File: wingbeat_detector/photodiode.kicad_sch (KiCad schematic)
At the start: 5 parts, among them U4 OPA381

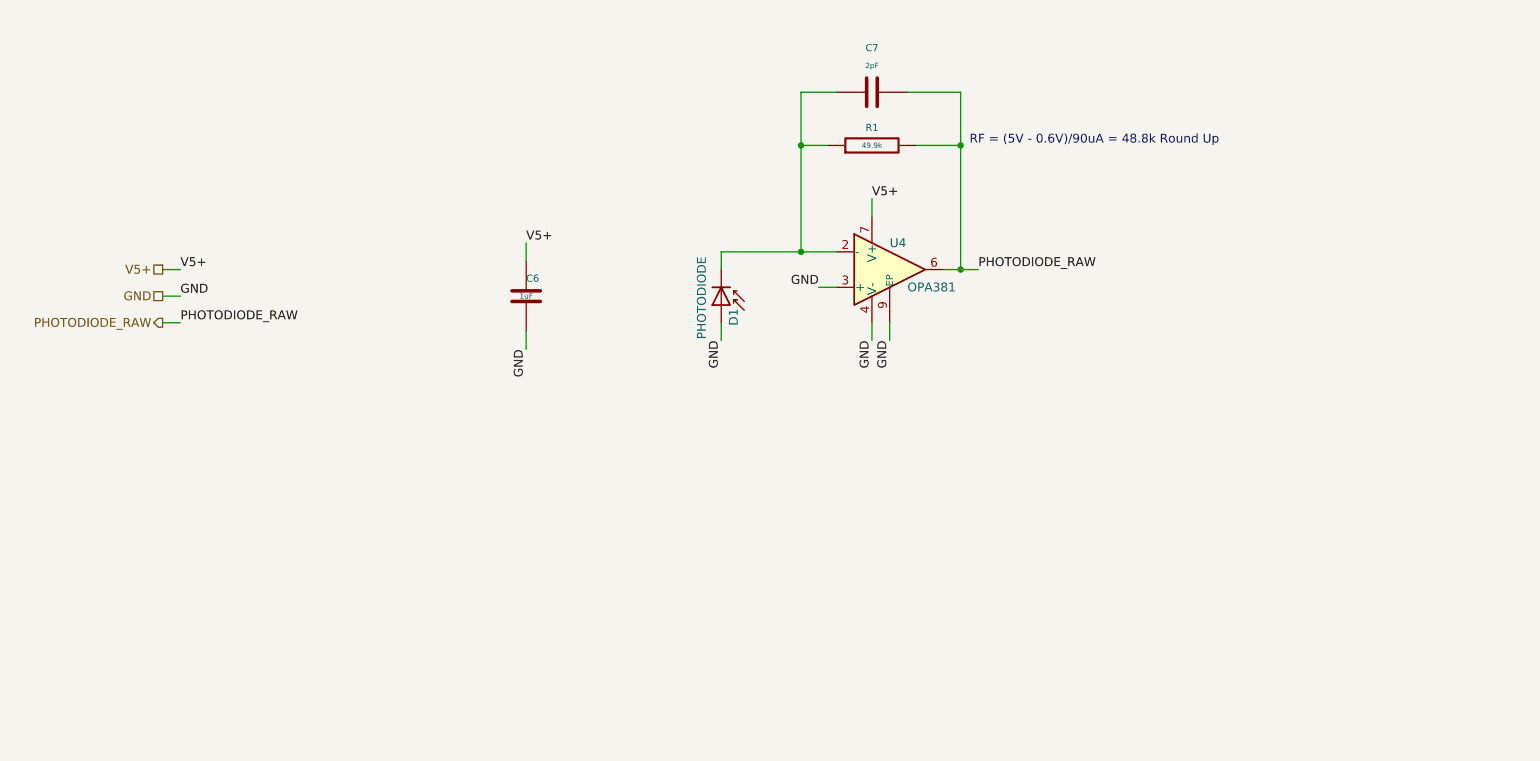
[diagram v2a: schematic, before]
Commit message: Add buffered output
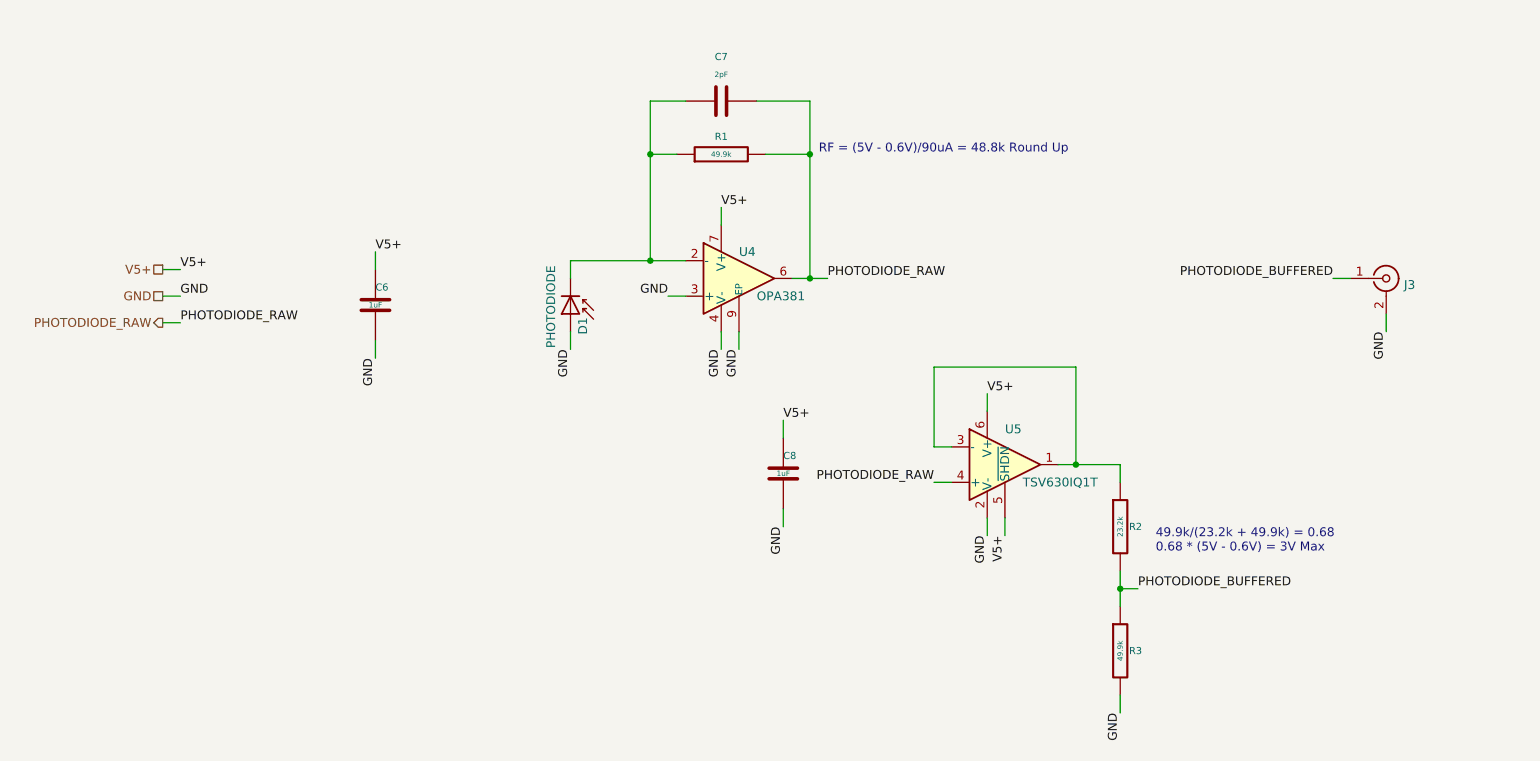
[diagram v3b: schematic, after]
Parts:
- added C8: 1uF, Janelia:C_0402_1005Metric, symbol Janelia:C_1uF_0402
- added J3: CONN_UMC_JACK_SMD, Janelia:UMC_AMPHENOL_A-1JB, symbol Janelia:CONN_UMC_JACK_SMD
- added R2: 23.2k, Janelia:R_0402_1005Metric, symbol Janelia:R_23.2k_0402
- added R3: 49.9k, Janelia:R_0402_1005Metric, symbol Janelia:R_49.9k_0402
- added U5: TSV630IQ1T, Janelia:PSON40P120X130X50-6N, symbol Janelia:TSV630IQ1T
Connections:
- net GND: now also C8.2, J3.2 (Ext), R3.2, U5.2 (V-)
- net PHOTODIODE_RAW: now also U5.4 (+)
- net V5+: now also C8.1, U5.5 (~{SHDN}), U5.6 (V+)
- new net: R2.1, U5.1, U5.3 (-)
- new net PHOTODIODE_BUFFERED: J3.1 (In), R2.2, R3.1
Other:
- note added: "49.9k/(23.2k + 49.9k) = 0.68 0.68 * (5V - 0.6V) = 3V Max"
- company: (none) -> Howard Hughes Medical Institute
- title: (none) -> wingbeat_detector
- moved on the sheet: C6, C7, D1, R1, U4

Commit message: Initial schematic layout
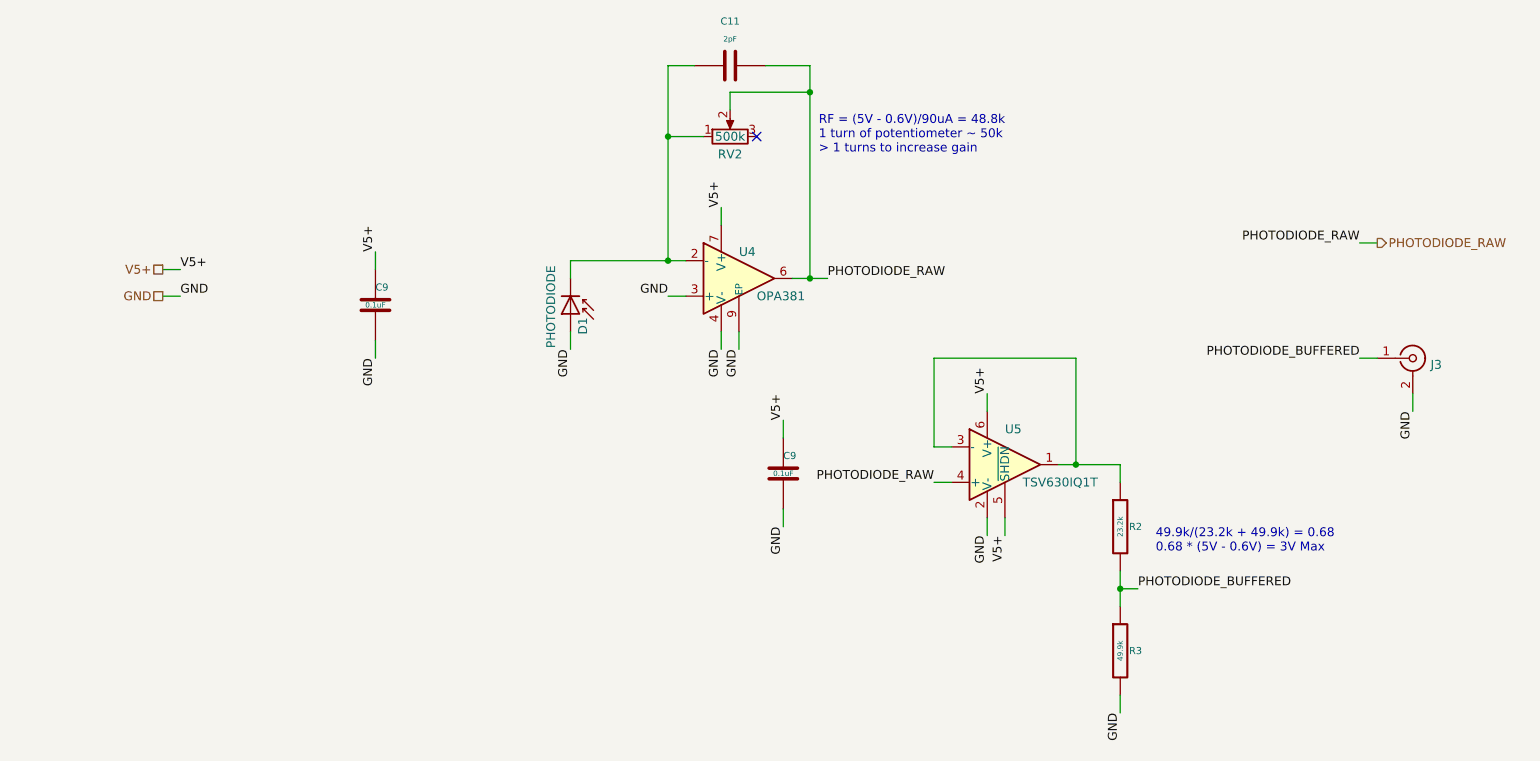
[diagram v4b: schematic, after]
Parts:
- removed C6, C8: 1uF, Janelia:C_0402_1005Metric, symbol Janelia:C_1uF_0402
- removed R1: 49.9k, Janelia:R_0402_1005Metric, symbol Janelia:R_49.9k_0402
- added C9 (x2): 0.1uF, Janelia:C_0402_1005Metric, symbol Janelia:C_0.1uF_0402
- added RV2: 500k, Janelia:Potentiometer_Bourns_3223W_Vertical, symbol Janelia:R_Potentiometer_500k_3.9x3.18mm_11turn_Vertical
- renumbered C7 to C11
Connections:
- net GND: now also C9.2, C9.2
- net PHOTODIODE_RAW: now also RV2.2
- net V5+: now also C9.1, C9.1
- net at C11.1, D1.1 (K), U4.2 (-): now also RV2.1
- no-connect marks 0 -> 1
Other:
- note added: "RF = (5V - 0.6V)/90uA = 48.8k 1 turn of potentiometer ~ 50k > 1 turns to increase gain"
- note removed: "RF = (5V - 0.6V)/90uA = 48.8k Round Up"
- moved on the sheet: C11, J3

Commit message: Double check schematic
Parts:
- added R3 (x3): 49.9k, Janelia:R_0402_1005Metric, symbol Janelia:R_49.9k_0402
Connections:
- net GND: now also R3.1
- net PHOTODIODE_RAW: now also R3.2
- new net: R3.1, R3.1, R3.2
- new net V10-: R3.2
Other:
- note added: "Optional pulldown resistor to ~ -5V to extend output voltage range to include 0V"
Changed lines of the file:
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@@
   (junction (at 186.69 111.76) (diameter 0) (color 0 0 0 0)
+  )
+  (junction (at 86.36 125.73) (diameter 0) (color 0 0 0 0)
   )
   (junction (at 128.27 64.77) (diameter 0) (color 0 0 0 0)
@@
     (stroke (width 0) (type default))
   )
+  (wire (pts (xy 86.36 125.73) (xy 86.36 128.27))
+    (stroke (width 0) (type default))
+  )
   (wire (pts (xy 138.43 92.71) (xy 138.43 95.25))
     (stroke (width 0) (type default))
@@
     (stroke (width 0) (type default))
   )
+  (wire (pts (xy 101.6 125.73) (xy 104.14 125.73))
+    (stroke (width 0) (type default))
+  )
   (wire (pts (xy 132.08 54.61) (xy 128.27 54.61))
     (stroke (width 0) (type default))
@@
     (stroke (width 0) (type default))
   )
+  (wire (pts (xy 55.88 91.44) (xy 58.42 91.44))
+    (stroke (width 0) (type default))
+  )
   (wire (pts (xy 173.99 104.14) (xy 173.99 101.6))
     (stroke (width 0) (type default))
@@
     (stroke (width 0) (type default))
   )
+  (wire (pts (xy 86.36 140.97) (xy 86.36 143.51))
+    (stroke (width 0) (type default))
+  )
   (wire (pts (xy 173.99 119.38) (xy 173.99 121.92))
     (stroke (width 0) (type default))
   )
+  (wire (pts (xy 86.36 123.19) (xy 86.36 125.73))
+    (stroke (width 0) (type default))
+  )
   (wire (pts (xy 186.69 111.76) (xy 193.04 111.76))
     (stroke (width 0) (type default))
@@
   )
   (wire (pts (xy 114.3 82.55) (xy 128.27 82.55))
+    (stroke (width 0) (type default))
+  )
+  (wire (pts (xy 86.36 110.49) (xy 86.36 107.95))
+    (stroke (width 0) (type default))
+  )
+  (wire (pts (xy 86.36 125.73) (xy 88.9 125.73))
     (stroke (width 0) (type default))
   )
@@
     (effects (font (size 1.27 1.27)) (justify left bottom))
   )
+  (text "Optional pulldown resistor to ~ -5V\nto extend output voltage range to \ninclude 0V"
+    (at 92.71 135.89 0)
+    (effects (font (size 1.27 1.27)) (justify left bottom))
+  )
   (label "V5+" (at 135.89 74.93 90) (fields_autoplaced)
     (effects (font (size 1.27 1.27)) (justify left bottom))
@@
     (effects (font (size 1.27 1.27)) (justify right bottom))
   )
+  (label "PHOTODIODE_RAW" (at 104.14 125.73 0) (fields_autoplaced)
+    (effects (font (size 1.27 1.27)) (justify left bottom))
+  )
   (label "V5+" (at 86.36 81.28 90) (fields_autoplaced)
     (effects (font (size 1.27 1.27)) (justify left bottom))
@@
     (effects (font (size 1.27 1.27)) (justify right bottom))
   )
+  (label "V10-" (at 86.36 143.51 270) (fields_autoplaced)
+    (effects (font (size 1.27 1.27)) (justify right bottom))
+  )
   (label "GND" (at 86.36 96.52 270) (fields_autoplaced)
     (effects (font (size 1.27 1.27)) (justify right bottom))
@@
     (effects (font (size 1.27 1.27)) (justify right bottom))
   )
+  (label "GND" (at 86.36 107.95 90) (fields_autoplaced)
+    (effects (font (size 1.27 1.27)) (justify left bottom))
+  )
   (label "GND" (at 58.42 87.63 0) (fields_autoplaced)
     (effects (font (size 1.27 1.27)) (justify left bottom))
@@
   (label "PHOTODIODE_BUFFERED" (at 227.33 96.52 180) (fields_autoplaced)
     (effects (font (size 1.27 1.27)) (justify right bottom))
+  )
+  (label "V10-" (at 58.42 91.44 0) (fields_autoplaced)
+    (effects (font (size 1.27 1.27)) (justify left bottom))
   )
   (label "V5+" (at 173.99 101.6 90) (fields_autoplaced)
@@
     (effects (font (size 1.27 1.27)) (justify left))
   )
+  (hierarchical_label "V10-" (shape passive) (at 55.88 91.44 180) (fields_autoplaced)
+    (effects (font (size 1.27 1.27)) (justify right))
+  )
   (hierarchical_label "V5+" (shape passive) (at 55.88 83.82 180) (fields_autoplaced)
     (effects (font (size 1.27 1.27)) (justify right))
@@
     (effects (font (size 1.27 1.27)) (justify right))
   )
+  (symbol (lib_id "Janelia:R_49.9k_0402") (at 86.36 116.84 0) (unit 1)
+    (in_bom yes) (on_board yes) (dnp no)
+    (property "Reference" "R3" (at 87.63 116.84 0)
+      (effects (font (size 1.016 1.016)) (justify left))
+    )
+    (property "Value" "49.9k" (at 86.36 116.84 90)
+      (effects (font (size 0.762 0.762)))
+    )
+    (property "Footprint" "Janelia:R_0402_1005Metric" (at 84.582 116.84 90)
+      (effects (font (size 0.762 0.762)) hide)
+    )
+    (property "Datasheet" "" (at 88.392 116.84 90)
+      (effects (font (size 0.762 0.762)))
+    )
+    (property "Vendor" "Digi-Key" (at 90.932 114.3 90)
+      (effects (font (size 1.524 1.524)) hide)
+    )
+    (property "Vendor Part Number" "P49.9KLCT-ND" (at 93.472 111.76 90)
+      (effects (font (size 1.524 1.524)) hide)
+    )
+    (property "Description" "RES SMD 49.9K OHM 1% 1/10W" (at 96.012 109.22 90)
+      (effects (font (size 1.524 1.524)) hide)
+    )
+    (property "Package" "0402" (at 86.36 116.84 0)
+      (effects (font (size 1.27 1.27)) hide)
+    )
+    (property "Manufacturer" "Panasonic Electronic Components" (at 86.36 116.84 0)
+      (effects (font (size 1.27 1.27)) hide)
+    )
+    (property "Manufacturer Part Number" "ERJ-2RKF4992X" (at 86.36 116.84 0)
+      (effects (font (size 1.27 1.27)) hide)
+    )
+    (pin "1")
+    (pin "2")
+    (instances
+      (project "wingbeat_detector"
+        (path "/cc457ebc-4af6-4663-b19f-8cb38f061cb4/669b71f5-24db-4526-af56-a5891b9eda40"
+          (reference "R3") (unit 1)
+        )
+        (path "/cc457ebc-4af6-4663-b19f-8cb38f061cb4/6f9841bf-b0ef-48ff-bf2c-2bd611c72bf3"
+          (reference "R10") (unit 1)
+        )
+      )
+    )
+  )
+  (symbol (lib_id "Janelia:R_49.9k_0402") (at 86.36 134.62 0) (unit 1)
+    (in_bom yes) (on_board yes) (dnp no)
+    (property "Reference" "R3" (at 87.63 134.62 0)
+      (effects (font (size 1.016 1.016)) (justify left))
+    )
+    (property "Value" "49.9k" (at 86.36 134.62 90)
+      (effects (font (size 0.762 0.762)))
+    )
+    (property "Footprint" "Janelia:R_0402_1005Metric" (at 84.582 134.62 90)
+      (effects (font (size 0.762 0.762)) hide)
+    )
+    (property "Datasheet" "" (at 88.392 134.62 90)
+      (effects (font (size 0.762 0.762)))
+    )
+    (property "Vendor" "Digi-Key" (at 90.932 132.08 90)
+      (effects (font (size 1.524 1.524)) hide)
+    )
+    (property "Vendor Part Number" "P49.9KLCT-ND" (at 93.472 129.54 90)
+      (effects (font (size 1.524 1.524)) hide)
+    )
+    (property "Description" "RES SMD 49.9K OHM 1% 1/10W" (at 96.012 127 90)
+      (effects (font (size 1.524 1.524)) hide)
+    )
+    (property "Package" "0402" (at 86.36 134.62 0)
+      (effects (font (size 1.27 1.27)) hide)
+    )
+    (property "Manufacturer" "Panasonic Electronic Components" (at 86.36 134.62 0)
+      (effects (font (size 1.27 1.27)) hide)
+    )
+    (property "Manufacturer Part Number" "ERJ-2RKF4992X" (at 86.36 134.62 0)
+      (effects (font (size 1.27 1.27)) hide)
+    )
+    (pin "1")
+    (pin "2")
+    (instances
+      (project "wingbeat_detector"
+        (path "/cc457ebc-4af6-4663-b19f-8cb38f061cb4/669b71f5-24db-4526-af56-a5891b9eda40"
+          (reference "R3") (unit 1)
+        )
+        (path "/cc457ebc-4af6-4663-b19f-8cb38f061cb4/6f9841bf-b0ef-48ff-bf2c-2bd611c72bf3"
+          (reference "R11") (unit 1)
+        )
+      )
+    )
+  )
   (symbol (lib_id "Janelia:C_0.1uF_0402") (at 86.36 88.9 0) (unit 1)
     (in_bom yes) (on_board yes) (dnp no)
@@
         )
         (path "/cc457ebc-4af6-4663-b19f-8cb38f061cb4/6f9841bf-b0ef-48ff-bf2c-2bd611c72bf3"
-          (reference "R10") (unit 1)
+          (reference "R13") (unit 1)
         )
       )
@@
         )
         (path "/cc457ebc-4af6-4663-b19f-8cb38f061cb4/6f9841bf-b0ef-48ff-bf2c-2bd611c72bf3"
-          (reference "R11") (unit 1)
+          (reference "R14") (unit 1)
         )
       )
@@
         )
       )
+    )
+  )
+  (symbol (lib_id "Janelia:R_49.9k_0402") (at 95.25 125.73 90) (unit 1)
+    (in_bom yes) (on_board yes) (dnp no)
+    (property "Reference" "R3" (at 95.25 124.46 0)
+      (effects (font (size 1.016 1.016)) (justify left))
+    )
+    (property "Value" "49.9k" (at 95.25 125.73 90)
+      (effects (font (size 0.762 0.762)))
+    )
+    (property "Footprint" "Janelia:R_0402_1005Metric" (at 95.25 127.508 90)
+      (effects (font (size 0.762 0.762)) hide)
+    )
+    (property "Datasheet" "" (at 95.25 123.698 90)
+      (effects (font (size 0.762 0.762)))
+    )
+    (property "Vendor" "Digi-Key" (at 92.71 121.158 90)
+      (effects (font (size 1.524 1.524)) hide)
+    )
+    (property "Vendor Part Number" "P49.9KLCT-ND" (at 90.17 118.618 90)
+      (effects (font (size 1.524 1.524)) hide)
+    )
+    (property "Description" "RES SMD 49.9K OHM 1% 1/10W" (at 87.63 116.078 90)
+      (effects (font (size 1.524 1.524)) hide)
+    )
+    (property "Package" "0402" (at 95.25 125.73 0)
+      (effects (font (size 1.27 1.27)) hide)
+    )
+    (property "Manufacturer" "Panasonic Electronic Components" (at 95.25 125.73 0)
+      (effects (font (size 1.27 1.27)) hide)
+    )
+    (property "Manufacturer Part Number" "ERJ-2RKF4992X" (at 95.25 125.73 0)
+      (effects (font (size 1.27 1.27)) hide)
+    )
+    (pin "1")
+    (pin "2")
+    (instances
+      (project "wingbeat_detector"
+        (path "/cc457ebc-4af6-4663-b19f-8cb38f061cb4/669b71f5-24db-4526-af56-a5891b9eda40"
+          (reference "R3") (unit 1)
+        )
+        (path "/cc457ebc-4af6-4663-b19f-8cb38f061cb4/6f9841bf-b0ef-48ff-bf2c-2bd611c72bf3"
+          (reference "R12") (unit 1)
+        )
+      )

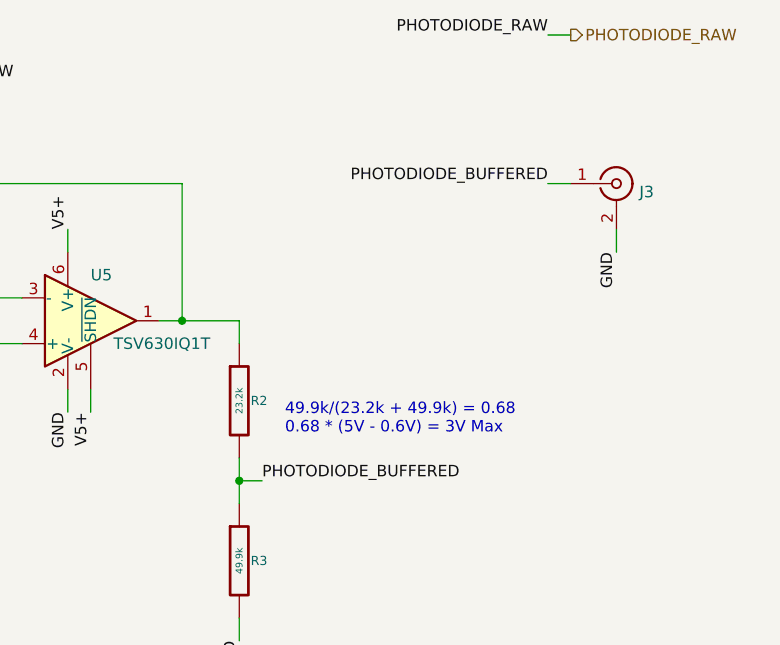
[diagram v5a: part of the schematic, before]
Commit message: Rearrange pcb footprints
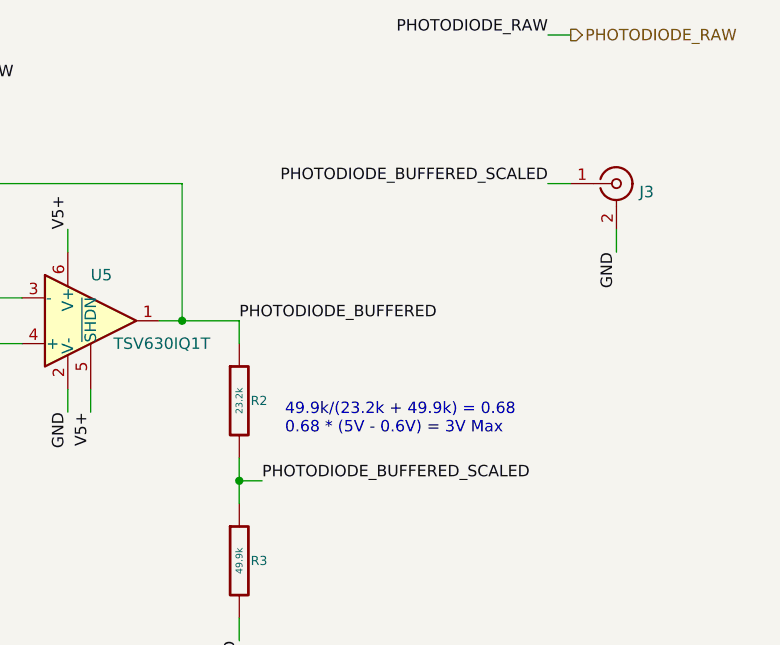
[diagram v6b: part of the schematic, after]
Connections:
- net PHOTODIODE_BUFFERED: now also R2.1, U5.1, U5.3 (-); no longer J3.1 (In), R2.2, R3.1
- new net PHOTODIODE_BUFFERED_SCALED: J3.1 (In), R2.2, R3.1
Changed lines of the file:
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@@
   (title_block
     (title "wingbeat_detector")
+    (date "2023-03-17")
     (rev "3.0")
     (company "Howard Hughes Medical Institute")
@@
     (effects (font (size 1.27 1.27)) (justify left bottom))
   )
-  (label "PHOTODIODE_BUFFERED" (at 195.58 129.54 0) (fields_autoplaced)
+  (label "PHOTODIODE_BUFFERED_SCALED" (at 195.58 129.54 0) (fields_autoplaced)
     (effects (font (size 1.27 1.27)) (justify left bottom))
   )
@@
     (effects (font (size 1.27 1.27)) (justify left bottom))
   )
-  (label "PHOTODIODE_BUFFERED" (at 227.33 96.52 180) (fields_autoplaced)
-    (effects (font (size 1.27 1.27)) (justify right bottom))
+  (label "PHOTODIODE_BUFFERED_SCALED" (at 227.33 96.52 180) (fields_autoplaced)
+    (effects (font (size 1.27 1.27)) (justify right bottom))
+  )
+  (label "PHOTODIODE_BUFFERED" (at 193.04 111.76 0) (fields_autoplaced)
+    (effects (font (size 1.27 1.27)) (justify left bottom))
   )
   (label "V10-" (at 58.42 91.44 0) (fields_autoplaced)
